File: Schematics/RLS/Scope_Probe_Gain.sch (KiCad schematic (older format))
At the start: 3 parts

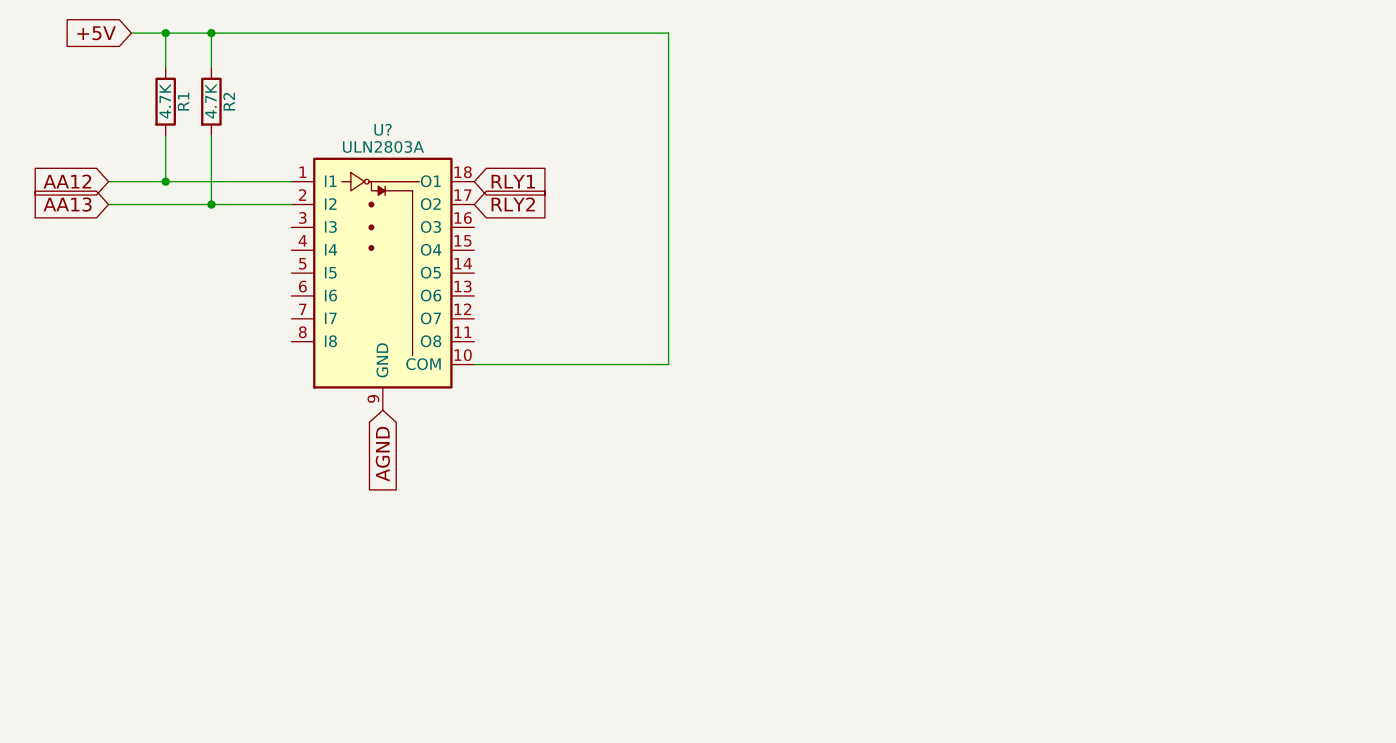
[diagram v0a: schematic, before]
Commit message: Updated Regulator Circuits and Fixed Velleman Gain
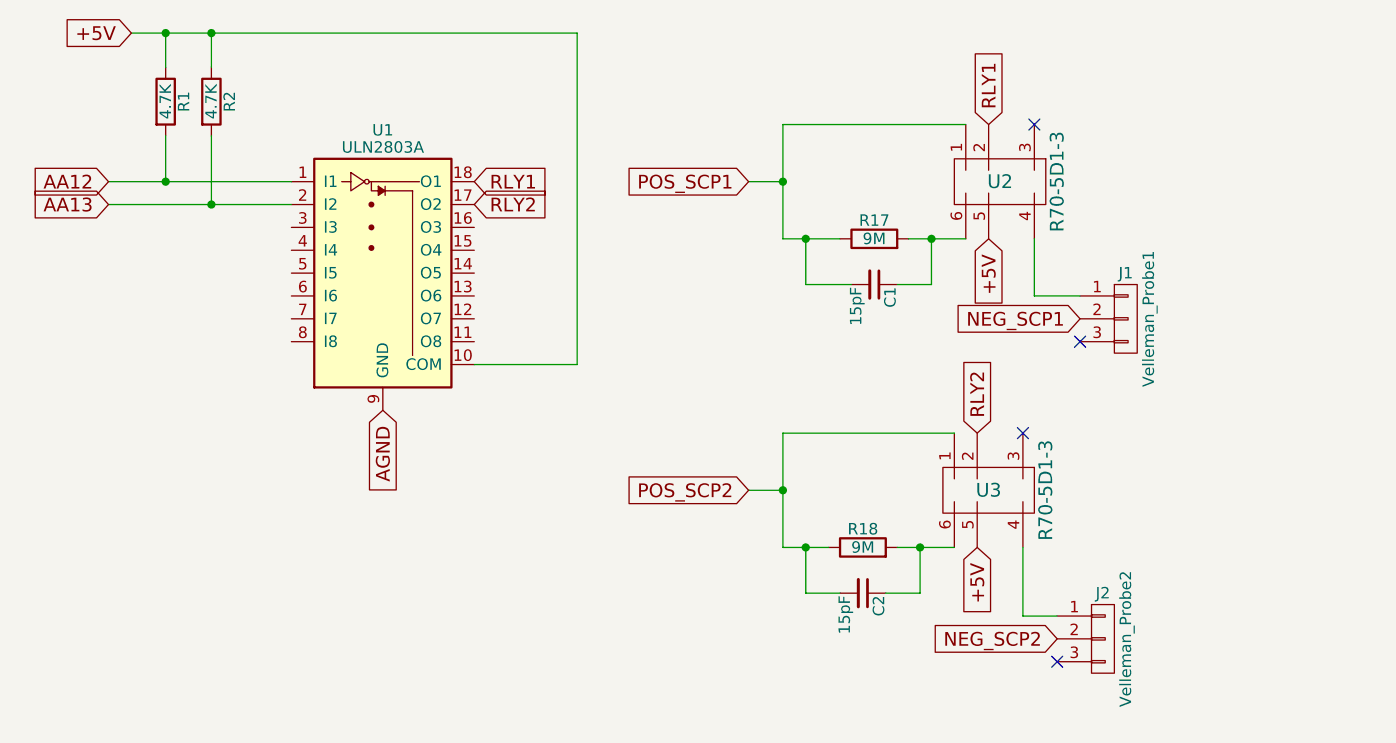
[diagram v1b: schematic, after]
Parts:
- added C1, C2: 15pF, symbol C_Small
- added J1: Velleman_Probe1, symbol CONN_01X03
- added J2: Velleman_Probe2, symbol CONN_01X03
- added R17, R18: 9M, symbol R
- added U2, U3: R70-5D1-3, symbol R70-5D1-3
- gave numbers to parts that had none: 1
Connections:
- net +5V: now also U2.5, U3.5
- net RLY1: now also U2.2
- net RLY2: now also U3.2
- new net: J1.1 (P1), U2.4
- new net: C1.1, R17.2, U2.6
- new net: J2.1 (P1), U3.4
- new net: C2.1, R18.2, U3.6
- new net NEG_SCP1: J1.2 (P2)
- new net NEG_SCP2: J2.2 (P2)
- new net POS_SCP1: C1.2, R17.1, U2.1
- new net POS_SCP2: C2.2, R18.1, U3.1
- no-connect marks 0 -> 4
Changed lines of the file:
@@
 EESchema Schematic File Version 2
+LIBS:RLS-rescue
 LIBS:power
 LIBS:device
@@
 $EndDescr
 $Comp
-L ULN2803A U?
+L ULN2803A U1
 U 1 1 594DCBE5
 P 4450 1900
-F 0 "U?" H 4450 2425 50  0000 C CNN
+F 0 "U1" H 4450 2425 50  0000 C CNN
 F 1 "ULN2803A" H 4450 2350 50  0000 C CNN
 F 2 "" H 4500 1250 50  0001 L CNN
@@
 	1    0    0    -1
 $EndComp
-Wire Wire Line
-	4850 2400 5700 2400
-Wire Wire Line
-	5700 2400 5700 950
-Wire Wire Line
-	5700 950  3350 950
+Text GLabel 4850 1600 2    60   Input ~ 0
+RLY1
+Text GLabel 4850 1700 2    60   Input ~ 0
+RLY2
+$Comp
+L R70-5D1-3 U2
+U 1 1 595850A9
+P 7250 1800
+F 0 "U2" H 7350 2000 60  0000 C CNN
+F 1 "R70-5D1-3" V 7100 2000 60  0000 C CNN
+F 2 "" H 7250 1800 60  0001 C CNN
+F 3 "" H 7250 1800 60  0001 C CNN
+	1    7250 1800
+	-1   0    0    -1
+$EndComp
+$Comp
+L R70-5D1-3 U3
+U 1 1 59585156
+P 7200 3150
+F 0 "U3" H 7300 3350 60  0000 C CNN
+F 1 "R70-5D1-3" V 7050 3350 60  0000 C CNN
+F 2 "" H 7200 3150 60  0001 C CNN
+F 3 "" H 7200 3150 60  0001 C CNN
+	1    7200 3150
+	-1   0    0    -1
+$EndComp
+Text GLabel 6050 1600 0    60   Input ~ 0
+POS_SCP1
+Text GLabel 6050 2950 0    60   Input ~ 0
+POS_SCP2
+Text GLabel 7500 2200 0    60   Input ~ 0
+NEG_SCP1
+Text GLabel 7400 3600 0    60   Input ~ 0
+NEG_SCP2
+$Comp
+L R R17
+U 1 1 595881BF
+P 6600 1850
+F 0 "R17" V 6680 1850 50  0000 C CNN
+F 1 "9M" V 6600 1850 50  0000 C CNN
+F 2 "" V 6530 1850 50  0001 C CNN
+F 3 "" H 6600 1850 50  0001 C CNN
+	1    6600 1850
+	0    -1   -1   0
+$EndComp
+$Comp
+L R R18
+U 1 1 59588224
+P 6550 3200
+F 0 "R18" V 6630 3200 50  0000 C CNN
+F 1 "9M" V 6550 3200 50  0000 C CNN
+F 2 "" V 6480 3200 50  0001 C CNN
+F 3 "" H 6550 3200 50  0001 C CNN
+	1    6550 3200
+	0    -1   -1   0
+$EndComp
+$Comp
+L C_Small C1
+U 1 1 595882C2
+P 6600 2050
+F 0 "C1" H 6610 2120 50  0000 L CNN
+F 1 "15pF" H 6610 1970 50  0000 L CNN
+F 2 "" H 6600 2050 50  0001 C CNN
+F 3 "" H 6600 2050 50  0001 C CNN
+	1    6600 2050
+	0    1    1    0
+$EndComp
+$Comp
+L C_Small C2
+U 1 1 595883A5
+P 6550 3400
+F 0 "C2" H 6560 3470 50  0000 L CNN
+F 1 "15pF" H 6560 3320 50  0000 L CNN
+F 2 "" H 6550 3400 50  0001 C CNN
+F 3 "" H 6550 3400 50  0001 C CNN
+	1    6550 3400
+	0    1    1    0
+$EndComp
+$Comp
+L CONN_01X03 J1
+U 1 1 595883FC
+P 7700 2200
+F 0 "J1" H 7700 2400 50  0000 C CNN
+F 1 "Velleman_Probe1" V 7800 2200 50  0000 C CNN
+F 2 "" H 7700 2200 50  0001 C CNN
+F 3 "" H 7700 2200 50  0001 C CNN
+	1    7700 2200
+	1    0    0    -1
+$EndComp
+$Comp
+L CONN_01X03 J2
+U 1 1 5958858D
+P 7600 3600
+F 0 "J2" H 7600 3800 50  0000 C CNN
+F 1 "Velleman_Probe2" V 7700 3600 50  0000 C CNN
+F 2 "" H 7600 3600 50  0001 C CNN
+F 3 "" H 7600 3600 50  0001 C CNN
+	1    7600 3600
+	1    0    0    -1
+$EndComp
+NoConn ~ 7250 2700
+NoConn ~ 7300 1350
+NoConn ~ 7500 2300
+NoConn ~ 7400 3700
+Text GLabel 7050 2700 1    60   Input ~ 0
+RLY2
+Text GLabel 7100 1350 1    60   Input ~ 0
+RLY1
+Text GLabel 7100 1850 3    60   Input ~ 0
++5V
+Text GLabel 7050 3200 3    60   Input ~ 0
++5V
+Wire Wire Line
+	4850 2400 5300 2400
+Wire Wire Line
+	5300 950  5300 2400
+Wire Wire Line
+	3350 950  5300 950
 Wire Wire Line
 	3700 1400 3700 1700
@@
 Connection ~ 3500 1600
 Connection ~ 3700 1700
-Text GLabel 4850 1600 2    60   Input ~ 0
-RLY1
-Text GLabel 4850 1700 2    60   Input ~ 0
-RLY2
+Wire Wire Line
+	7500 2100 7300 2100
+Wire Wire Line
+	7300 2100 7300 1850
+Wire Wire Line
+	7400 3500 7250 3500
+Wire Wire Line
+	7250 3500 7250 3200
+Wire Wire Line
+	6700 3200 6950 3200
+Wire Wire Line
+	6800 3200 6800 3400
+Wire Wire Line
+	6800 3400 6650 3400
+Connection ~ 6800 3200
+Wire Wire Line
+	6200 3200 6400 3200
+Wire Wire Line
+	6300 3200 6300 3400
+Wire Wire Line
+	6300 3400 6450 3400
+Wire Wire Line
+	6950 2700 6200 2700
+Wire Wire Line
+	6200 2700 6200 3200
+Connection ~ 6300 3200
+Wire Wire Line
+	6200 2950 6050 2950
+Connection ~ 6200 2950
+Wire Wire Line
+	6750 1850 7000 1850
+Wire Wire Line
+	6850 1850 6850 2050
+Wire Wire Line
+	6850 2050 6700 2050
+Connection ~ 6850 1850
+Wire Wire Line
+	6200 1850 6450 1850
+Wire Wire Line
+	6300 1850 6300 2050
+Wire Wire Line
+	6300 2050 6500 2050
+Wire Wire Line
+	6200 1350 6200 1850
+Wire Wire Line
+	6200 1350 7000 1350
+Connection ~ 6300 1850
+Wire Wire Line
+	6200 1600 6050 1600
+Connection ~ 6200 1600
 $EndSCHEMATC

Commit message: Updated Schematic (Almost Done)
Finished both variable regulator circuits, added connectors for LAs, added +/- 5 regulated circuit for DB +/- 5V (needs to be tested before PCB implementation), various renaming and labeling
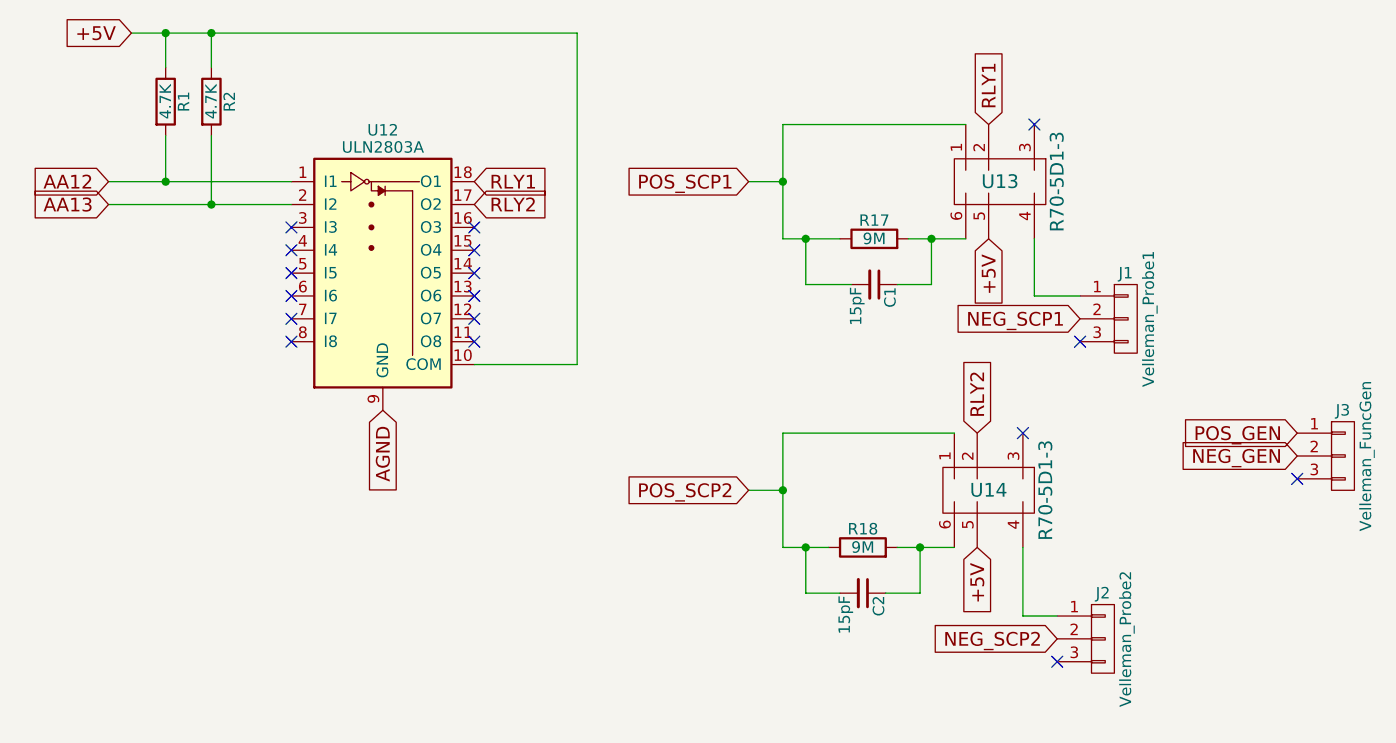
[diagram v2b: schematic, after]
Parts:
- added J3: Velleman_FuncGen, symbol CONN_01X03
- renumbered U1 to U12, U2 to U13, U3 to U14
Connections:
- new net NEG_GEN: J3.2 (P2)
- new net POS_GEN: J3.1 (P1)
- no-connect marks 4 -> 17
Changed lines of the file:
@@
 $Descr A4 11693 8268
 encoding utf-8
-Sheet 3 5
+Sheet 3 7
 Title ""
 Date ""
@@
 $EndDescr
 $Comp
-L ULN2803A U1
+L ULN2803A U12
 U 1 1 594DCBE5
 P 4450 1900
-F 0 "U1" H 4450 2425 50  0000 C CNN
+F 0 "U12" H 4450 2425 50  0000 C CNN
 F 1 "ULN2803A" H 4450 2350 50  0000 C CNN
 F 2 "" H 4500 1250 50  0001 L CNN
@@
 RLY2
 $Comp
-L R70-5D1-3 U2
+L R70-5D1-3 U13
 U 1 1 595850A9
 P 7250 1800
-F 0 "U2" H 7350 2000 60  0000 C CNN
+F 0 "U13" H 7350 2000 60  0000 C CNN
 F 1 "R70-5D1-3" V 7100 2000 60  0000 C CNN
 F 2 "" H 7250 1800 60  0001 C CNN
@@
 $EndComp
 $Comp
-L R70-5D1-3 U3
+L R70-5D1-3 U14
 U 1 1 59585156
 P 7200 3150
-F 0 "U3" H 7300 3350 60  0000 C CNN
+F 0 "U14" H 7300 3350 60  0000 C CNN
 F 1 "R70-5D1-3" V 7050 3350 60  0000 C CNN
 F 2 "" H 7200 3150 60  0001 C CNN
@@
 	4850 2400 5300 2400
 Wire Wire Line
-	5300 950  5300 2400
-Wire Wire Line
-	3350 950  5300 950
+	5300 2400 5300 950
+Wire Wire Line
+	5300 950  3350 950
 Wire Wire Line
 	3700 1400 3700 1700
@@
 	6200 1600 6050 1600
 Connection ~ 6200 1600
+$Comp
+L CONN_01X03 J3
+U 1 1 595A5435
+P 8650 2800
+F 0 "J3" H 8650 3000 50  0000 C CNN
+F 1 "Velleman_FuncGen" V 8750 2800 50  0000 C CNN
+F 2 "" H 8650 2800 50  0001 C CNN
+F 3 "" H 8650 2800 50  0001 C CNN
+	1    8650 2800
+	1    0    0    -1
+$EndComp
+Text GLabel 8450 2700 0    60   Input ~ 0
+POS_GEN
+Text GLabel 8450 2800 0    60   Input ~ 0
+NEG_GEN
+NoConn ~ 8450 2900
+NoConn ~ 4850 1800
+NoConn ~ 4850 1900
+NoConn ~ 4850 2000
+NoConn ~ 4850 2100
+NoConn ~ 4850 2200
+NoConn ~ 4850 2300
+NoConn ~ 4050 2300
+NoConn ~ 4050 2200
+NoConn ~ 4050 2100
+NoConn ~ 4050 2000
+NoConn ~ 4050 1900
+NoConn ~ 4050 1800
 $EndSCHEMATC

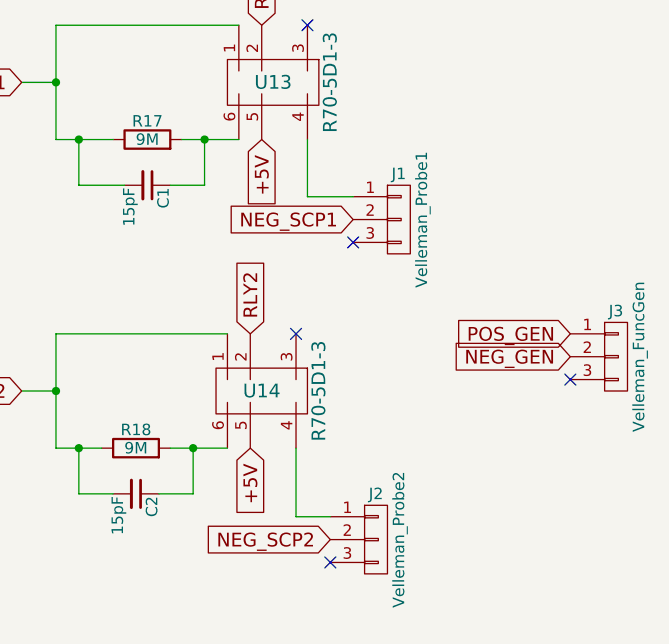
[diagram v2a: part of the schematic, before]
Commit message: Most Footprints Added
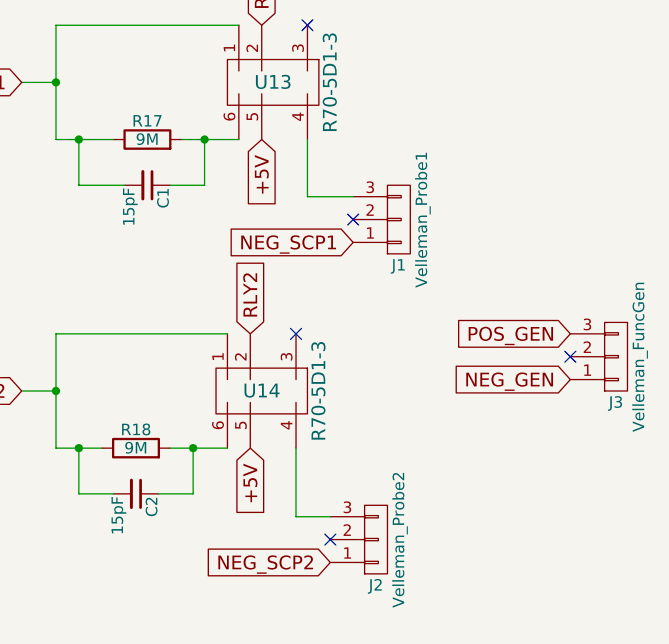
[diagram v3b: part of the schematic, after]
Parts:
- C1, C2: footprint (none) -> Capacitors_THT:C_Disc_D3.8mm_W2.6mm_P2.50mm
- J1, J2, J3: footprint (none) -> Pin_Headers:Pin_Header_Straight_1x03_Pitch2.54mm
- R1, R2: footprint (none) -> Resistors_SMD:R_0805_HandSoldering
- R17, R18: footprint (none) -> Resistors_THT:R_Axial_DIN0309_L9.0mm_D3.2mm_P12.70mm_Horizontal
- U12: footprint (none) -> Housings_DIP:DIP-18_W7.62mm
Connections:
- net NEG_GEN: now also J3.1 (P1); no longer J3.2 (P2)
- net NEG_SCP1: now also J1.1 (P1); no longer J1.2 (P2)
- net NEG_SCP2: now also J2.1 (P1); no longer J2.2 (P2)
- net POS_GEN: now also J3.3 (P3); no longer J3.1 (P1)
- net at U13.4: now also J1.3 (P3); no longer J1.1 (P1)
- net at U14.4: now also J2.3 (P3); no longer J2.1 (P1)
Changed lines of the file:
@@
 F 0 "U12" H 4450 2425 50  0000 C CNN
 F 1 "ULN2803A" H 4450 2350 50  0000 C CNN
-F 2 "" H 4500 1250 50  0001 L CNN
+F 2 "Housings_DIP:DIP-18_W7.62mm" H 4500 1250 50  0001 L CNN
 F 3 "" H 4550 1800 50  0001 C CNN
 	1    4450 1900
@@
 F 0 "R1" V 3580 1250 50  0000 C CNN
 F 1 "4.7K" V 3500 1250 50  0000 C CNN
-F 2 "" V 3430 1250 50  0001 C CNN
+F 2 "Resistors_SMD:R_0805_HandSoldering" V 3430 1250 50  0001 C CNN
 F 3 "" H 3500 1250 50  0001 C CNN
 	1    3500 1250
@@
 F 0 "R2" V 3780 1250 50  0000 C CNN
 F 1 "4.7K" V 3700 1250 50  0000 C CNN
-F 2 "" V 3630 1250 50  0001 C CNN
+F 2 "Resistors_SMD:R_0805_HandSoldering" V 3630 1250 50  0001 C CNN
 F 3 "" H 3700 1250 50  0001 C CNN
 	1    3700 1250
@@
 Text GLabel 6050 2950 0    60   Input ~ 0
 POS_SCP2
-Text GLabel 7500 2200 0    60   Input ~ 0
+Text GLabel 7500 2300 0    60   Input ~ 0
 NEG_SCP1
-Text GLabel 7400 3600 0    60   Input ~ 0
+Text GLabel 7400 3700 0    60   Input ~ 0
 NEG_SCP2
 $Comp
@@
 F 0 "R17" V 6680 1850 50  0000 C CNN
 F 1 "9M" V 6600 1850 50  0000 C CNN
-F 2 "" V 6530 1850 50  0001 C CNN
+F 2 "Resistors_THT:R_Axial_DIN0309_L9.0mm_D3.2mm_P12.70mm_Horizontal" V 6530 1850 50  0001 C CNN
 F 3 "" H 6600 1850 50  0001 C CNN
 	1    6600 1850
@@
 F 0 "R18" V 6630 3200 50  0000 C CNN
 F 1 "9M" V 6550 3200 50  0000 C CNN
-F 2 "" V 6480 3200 50  0001 C CNN
+F 2 "Resistors_THT:R_Axial_DIN0309_L9.0mm_D3.2mm_P12.70mm_Horizontal" V 6480 3200 50  0001 C CNN
 F 3 "" H 6550 3200 50  0001 C CNN
 	1    6550 3200
@@
 F 0 "C1" H 6610 2120 50  0000 L CNN
 F 1 "15pF" H 6610 1970 50  0000 L CNN
-F 2 "" H 6600 2050 50  0001 C CNN
+F 2 "Capacitors_THT:C_Disc_D3.8mm_W2.6mm_P2.50mm" H 6600 2050 50  0001 C CNN
 F 3 "" H 6600 2050 50  0001 C CNN
 	1    6600 2050
@@
 F 0 "C2" H 6560 3470 50  0000 L CNN
 F 1 "15pF" H 6560 3320 50  0000 L CNN
-F 2 "" H 6550 3400 50  0001 C CNN
+F 2 "Capacitors_THT:C_Disc_D3.8mm_W2.6mm_P2.50mm" H 6550 3400 50  0001 C CNN
 F 3 "" H 6550 3400 50  0001 C CNN
 	1    6550 3400
@@
 F 0 "J1" H 7700 2400 50  0000 C CNN
 F 1 "Velleman_Probe1" V 7800 2200 50  0000 C CNN
-F 2 "" H 7700 2200 50  0001 C CNN
+F 2 "Pin_Headers:Pin_Header_Straight_1x03_Pitch2.54mm" H 7700 2200 50  0001 C CNN
 F 3 "" H 7700 2200 50  0001 C CNN
 	1    7700 2200
-	1    0    0    -1
+	1    0    0    1
 $EndComp
 $Comp
@@
 F 0 "J2" H 7600 3800 50  0000 C CNN
 F 1 "Velleman_Probe2" V 7700 3600 50  0000 C CNN
-F 2 "" H 7600 3600 50  0001 C CNN
+F 2 "Pin_Headers:Pin_Header_Straight_1x03_Pitch2.54mm" H 7600 3600 50  0001 C CNN
 F 3 "" H 7600 3600 50  0001 C CNN
 	1    7600 3600
-	1    0    0    -1
+	1    0    0    1
 $EndComp
 NoConn ~ 7250 2700
 NoConn ~ 7300 1350
-NoConn ~ 7500 2300
-NoConn ~ 7400 3700
 Text GLabel 7050 2700 1    60   Input ~ 0
 RLY2
@@
 F 0 "J3" H 8650 3000 50  0000 C CNN
 F 1 "Velleman_FuncGen" V 8750 2800 50  0000 C CNN
-F 2 "" H 8650 2800 50  0001 C CNN
+F 2 "Pin_Headers:Pin_Header_Straight_1x03_Pitch2.54mm" H 8650 2800 50  0001 C CNN
 F 3 "" H 8650 2800 50  0001 C CNN
 	1    8650 2800
-	1    0    0    -1
+	1    0    0    1
 $EndComp
 Text GLabel 8450 2700 0    60   Input ~ 0
 POS_GEN
-Text GLabel 8450 2800 0    60   Input ~ 0
+Text GLabel 8450 2900 0    60   Input ~ 0
 NEG_GEN
-NoConn ~ 8450 2900
 NoConn ~ 4850 1800
 NoConn ~ 4850 1900
@@
 NoConn ~ 4050 1900
 NoConn ~ 4050 1800
+NoConn ~ 7400 3600
+NoConn ~ 8450 2800
+NoConn ~ 7500 2200
 $EndSCHEMATC
